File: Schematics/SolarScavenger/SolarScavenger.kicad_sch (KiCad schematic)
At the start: 47 parts, among them J1 SolarConnector, J10 CH1_OUT, J11 CH2_OUT, J12 CH3_OUT, J13 CH4_OUT, J2 PROGRAMMING, J3 BatteryPack, J4 ESC_PWM_CONTROL, J5 ESC_connector, J6 CH1_IN, J7 CH2_IN, J8 CH3_IN, J9 CH4_IN, Q1 IRLML2502, Q2 IRLML2502, U1 4N25, U2 AP1117-33, U3 ESP32-WROOM-E, U4 INA219AxD

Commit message: Schematic update
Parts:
- added J9: SPARES, Connector_PinHeader_2.54mm:PinHeader_1x03_P2.54mm_Vertical, symbol Connector_Generic:Conn_01x03
- added R4: 4k7, Resistor_SMD:R_1020_2550Metric_Pad1.33x5.20mm_HandSolder, symbol Device:R
- added U1: DS18B20, Package_TO_SOT_THT:TO-92_Inline, symbol Sensor_Temperature:DS18B20
- J6: renamed from J?; footprint (none) -> microSD:microSD-Receptacle-SelfEject
- R5: renamed from R?; footprint (none) -> Connector_PinHeader_2.54mm:PinHeader_1x02_P2.54mm_Vertical
- gave numbers to parts that had none: 7
- renumbered J6 to J10, J7 to J11, J8 to J12, J9 to J13, J10 to J14, J11 to J15, J12 to J16, J13 to J17, R2 to R1, R6 to R13, R7 to R14, R8 to R15, R9 to R16, R10 to R17, R11 to R18, R12 to R19, R3 to R2, R1 to R3, R4 to R6, R5 to R7, U1 to U2, U2 to U3, U3 to U4, U4 to U5
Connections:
- net SPARE_GPI12 is gone; now on net SD_DATA2: U4.14 (MTDI/GPIO12/ADC2_CH5)
- net SPARE_GPI13 is gone; now on net SD_DATA3: U4.16 (MTCK/GPIO13/ADC2_CH4)
- net SPARE_GPI14 is gone; now on net SD_CLK: U4.13 (MTMS/GPIO14/ADC2_CH6)
- net SPARE_GPI15 is gone; now on net SD_CMD: U4.23 (MTDO/GPIO15/ADC2_CH3)
- net SPARE_GPI25 is gone; now on net RUDDER_ADC: U4.10 (DAC_1/ADC2_CH8/GPIO25)
- net SPARE_GPI26 is gone; now on net THROTTLE_ADC: U4.11 (DAC_2/ADC2_CH9/GPIO26)
- net +3V3: now also R4.1, U1.3 (VDD)
- net GND: now also J6.9 (SHIELD), R5.2, U1.1 (GND)
- net LED_1: now also U4.29 (GPIO5); no longer U4.6 (GPIO34/ADC1_CH6)
- net LED_2: now also U4.12 (ADC2_CH7/GPIO27); no longer U4.7 (GPIO35/ADC1_CH7)
- net RUDDER_ADC: no longer U4.24 (ADC2_CH2/GPIO2)
- net SD_DATA0: now also U4.24 (ADC2_CH2/GPIO2)
- net SD_DATA1: now also U4.26 (ADC2_CH0/GPIO4)
- net SPARE_GPI27: now also U4.6 (GPIO34/ADC1_CH6), J9.2 (Pin_2); no longer U4.12 (ADC2_CH7/GPIO27)
- net SPARE_GPI33: now also J9.3 (Pin_3)
- net SPARE_GPIO5: now also U4.7 (GPIO35/ADC1_CH7), J9.1 (Pin_1); no longer U4.29 (GPIO5)
- net THROTTLE_ADC: no longer U4.26 (ADC2_CH0/GPIO4)
- net LIGHT_SENSOR: now reaches R5.1
- net LIGHT_SENSOR: now also U4.5 (SENSOR_VN/GPIO39/ADC1_CH3), R4.2
- net SD_CLK: now reaches J6.5 (CLK)
- net SPARE_GPI32 renamed TEMP_SESNOR
- net TEMP_SESNOR: now also U1.2 (DQ)
- no-connect marks 0 -> 1
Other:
- company: (none) -> @LabGluon y @Prediktor
- title: (none) -> Solar Scavenger
- moved on the sheet: D1, D2, J6, JP1, Q1, Q2, R1, R10, R11, R12, R2, R5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

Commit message: PCB final candidate
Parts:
- removed J9: SPARES, Connector_PinHeader_2.54mm:PinHeader_1x03_P2.54mm_Vertical, symbol Connector_Generic:Conn_01x03
- added JP6: INA_A0, Jumper:SolderJumper-2_P1.3mm_Open_Pad1.0x1.5mm, symbol Jumper:SolderJumper_2_Open
- added JP7: INA_A1, Jumper:SolderJumper-2_P1.3mm_Open_Pad1.0x1.5mm, symbol Jumper:SolderJumper_2_Open
- added R20: 47k, Resistor_SMD:R_1206_3216Metric_Pad1.30x1.75mm_HandSolder, symbol Device:R
- D1, D2: footprint LED_THT:LED_D5.0mm -> LED_SMD:LED_1210_3225Metric_Pad1.42x2.65mm_HandSolder
- R10, R11, R12, R13, R14, R15, R16, R17, R4, R7, R8, R9: footprint Resistor_SMD:R_1020_2550Metric_Pad1.33x5.20mm_HandSolder -> Resistor_SMD:R_1206_3216Metric_Pad1.30x1.75mm_HandSolder
- U3: footprint Package_TO_SOT_SMD:SOT-223-3_TabPin2 -> Package_TO_SOT_THT:TO-220-3_Vertical
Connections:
- net +3V3: now also R16.2, JP6.1 (A), R20.2; no longer R16.1, U5.1 (A1), U5.2 (A0)
- net GND: now also J1.1 (Pin_1), J5.1 (Pin_1), J6.11 (SHIELD), JP7.1 (A); no longer J1.2 (Pin_2), J5.2 (Pin_2), J6.9 (SHIELD)
- net INA_SDA: now also R16.1; no longer R16.2
- net MOTOR_SUPPLY_P: now also J5.2 (Pin_2); no longer J5.1 (Pin_1)
- net SUPPLY_IN_P: now also J1.2 (Pin_2); no longer J1.1 (Pin_1)
- net SPARE_GPI27: no longer names the net of U4.6 (GPIO34/ADC1_CH6)
- net SPARE_GPI33 renamed /CD_DETECT
- net /CD_DETECT: now also J6.9 (CD), R20.1
- net SPARE_GPIO5: no longer names the net of U4.7 (GPIO35/ADC1_CH7)
- net TEMP_SESNOR renamed TEMP_SENSOR
- new net: JP6.2 (B), JP7.2 (B), U5.1 (A1), U5.2 (A0)
- no-connect marks 1 -> 3
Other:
- moved on the sheet: J1, J13, J17, JP5, R13, R14, R15, R17, R18, R19, U5

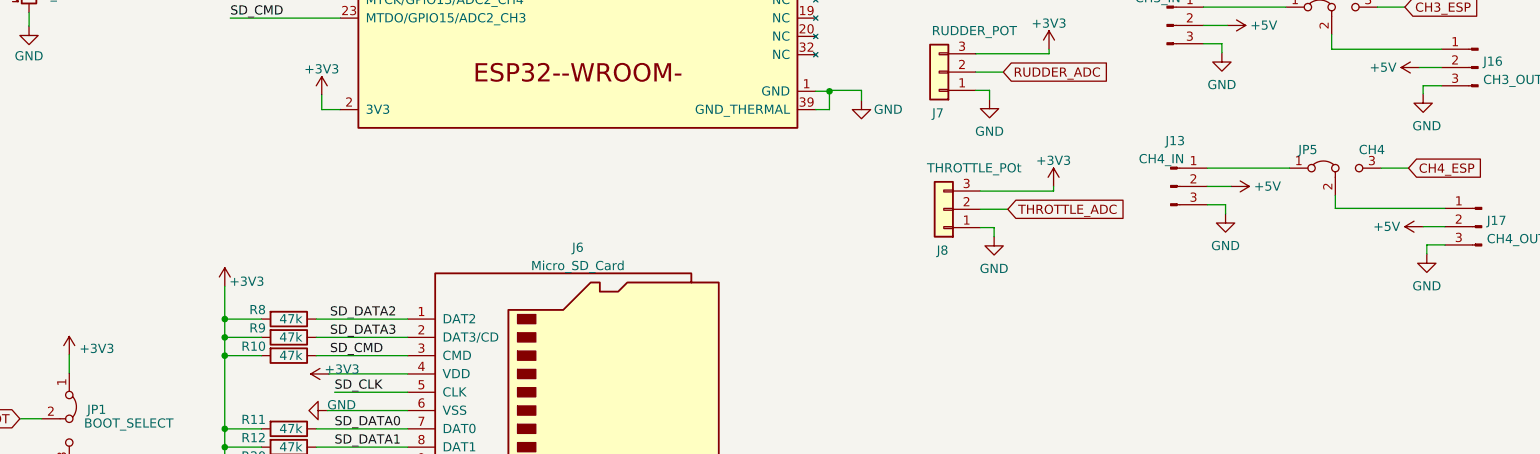
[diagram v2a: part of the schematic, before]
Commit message: Added SD writter and updated for IDF 5.0
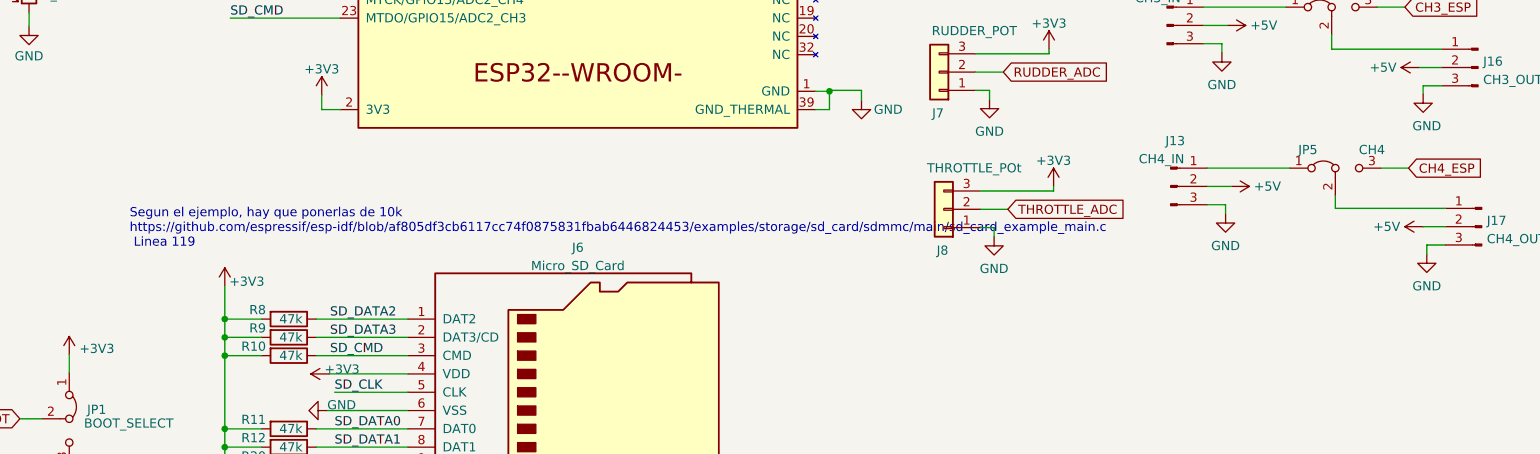
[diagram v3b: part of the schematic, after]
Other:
- note added: "Segun el ejemplo, hay que ponerlas de 10k https://github.com/espressif/esp-idf/blob/af805df3cb6117cc74f0875831fbab6446824453/examples/storage/sd_card/sdmmc/main/sd_card_example_main.c Linea 119"
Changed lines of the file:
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@@
     (stroke (width 0) (type default))
+  )
+  (text "Segun el ejemplo, hay que ponerlas de 10k\nhttps://github.com/espressif/esp-idf/blob/af805df3cb6117cc74f0875831fbab6446824453/examples/storage/sd_card/sdmmc/main/sd_card_example_main.c\n Linea 119"
+    (at 84.582 156.21 0)
+    (effects (font (size 1.27 1.27)) (justify left bottom))
   )
   (text "Máx: 22V, 6A" (at 17.78 27.432 0)

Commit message: PCB v1.1
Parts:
- removed J10: CH1_IN, Connector_PinHeader_2.54mm:PinHeader_1x03_P2.54mm_Vertical, symbol Connector:Conn_01x03_Male
- removed J11: CH2_IN, Connector_PinHeader_2.54mm:PinHeader_1x03_P2.54mm_Vertical, symbol Connector:Conn_01x03_Male
- removed J12: CH3_IN, Connector_PinHeader_2.54mm:PinHeader_1x03_P2.54mm_Vertical, symbol Connector:Conn_01x03_Male
- removed J13: CH4_IN, Connector_PinHeader_2.54mm:PinHeader_1x03_P2.54mm_Vertical, symbol Connector:Conn_01x03_Male
- removed J14: CH1_OUT, Connector_PinHeader_2.54mm:PinHeader_1x03_P2.54mm_Vertical, symbol Connector:Conn_01x03_Male
- removed J15: CH2_OUT, Connector_PinHeader_2.54mm:PinHeader_1x03_P2.54mm_Vertical, symbol Connector:Conn_01x03_Male
- removed J16: CH3_OUT, Connector_PinHeader_2.54mm:PinHeader_1x03_P2.54mm_Vertical, symbol Connector:Conn_01x03_Male
- removed J17: CH4_OUT, Connector_PinHeader_2.54mm:PinHeader_1x03_P2.54mm_Vertical, symbol Connector:Conn_01x03_Male
- removed J3: BatteryPack, Connector_PinHeader_2.54mm:PinHeader_1x02_P2.54mm_Vertical, symbol Connector_Generic:Conn_01x02
- removed JP2: CH1_MOTOR, Connector_PinHeader_2.54mm:PinHeader_1x03_P2.54mm_Vertical, symbol Jumper:Jumper_3_Bridged12
- removed JP3: CH2, Connector_PinHeader_2.54mm:PinHeader_1x03_P2.54mm_Vertical, symbol Jumper:Jumper_3_Bridged12
- removed JP4: CH3, Connector_PinHeader_2.54mm:PinHeader_1x03_P2.54mm_Vertical, symbol Jumper:Jumper_3_Bridged12
- removed JP5: CH4, Connector_PinHeader_2.54mm:PinHeader_1x03_P2.54mm_Vertical, symbol Jumper:Jumper_3_Bridged12
- removed Q1, Q2: IRLML2502, Package_TO_SOT_SMD:SOT-23_Handsoldering, symbol Transistor_FET:IRLZ44N
- removed U1: DS18B20, Package_TO_SOT_THT:TO-92_Inline, symbol Sensor_Temperature:DS18B20
- added C1, C3: 47uF, Capacitor_SMD:C_1206_3216Metric_Pad1.33x1.80mm_HandSolder, symbol Device:C_Small
- added C2, C4: 100nF, Capacitor_SMD:C_1206_3216Metric_Pad1.33x1.80mm_HandSolder, symbol Device:C_Small
- added J3: BATTERY, Connector_PinHeader_2.54mm:PinHeader_1x03_P2.54mm_Vertical, symbol Connector_Generic:Conn_01x03
- added Q1, Q3: IRLM2502, Package_TO_SOT_SMD:SOT-23, symbol GluonLib:IRLM2502
- added R21, R22: 1k, Resistor_SMD:R_1206_3216Metric_Pad1.30x1.75mm_HandSolder, symbol Device:R
- D1: value LED_1 -> LED_R
- D2: value LED_2 -> LED_G
- R1: value 300 -> 680
- R10, R12, R20, R8, R9: value 47k -> 10k
- R11: value 47k -> 10k; now not fitted
- R2: value 300 -> 2k2
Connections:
- net +3V3: now also C1.1, C3.1
- net GND: now also C1.2, C2.2, C3.2, C4.2, J3.1 (Pin_1), Q1.2 (S), Q3.2 (S), R22.2; no longer R7.1, U4.3 (EN/CHIP_PU)
- net LED_1: now also Q1.1 (G)
- net LED_2: now also Q3.1 (G)
- net MOTOR_VOLTAGE: now also C4.1
- net RUDDER_ADC: now also U4.6 (GPIO34/ADC1_CH6); no longer U4.10 (DAC_1/ADC2_CH8/GPIO25)
- net THROTTLE_ADC: now also U4.7 (GPIO35/ADC1_CH7); no longer U4.11 (DAC_2/ADC2_CH9/GPIO26)
- net at D1.1 (K): now also Q3.3 (D)
- net +BATT: now reaches U3.3 (VI)
- net +BATT: now also R1.1, R2.1, J3.2 (Pin_2), R21.1
- net at D2.1 (K): now also Q1.3 (D)
- net +5V renamed ESC_5V
- net ESC_5V: no longer R1.1, R2.1
- net TEMP_SENSOR renamed BATT_SENSOR
- net BATT_SENSOR: now also R21.2, R22.1
- new net: C2.1, R7.1, U4.3 (EN/CHIP_PU)
- no-connect marks 3 -> 4
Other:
- added sheet ServoConnections (servosConnections.kicad_sch)
- note added: "BATT: +Max: 5v5"
- moved on the sheet: D1, D2, J1, J2, J4, J5, J7, J8, JP1, R1, R14, R15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
